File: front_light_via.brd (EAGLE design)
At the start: 60 x 73 mm, 9 parts

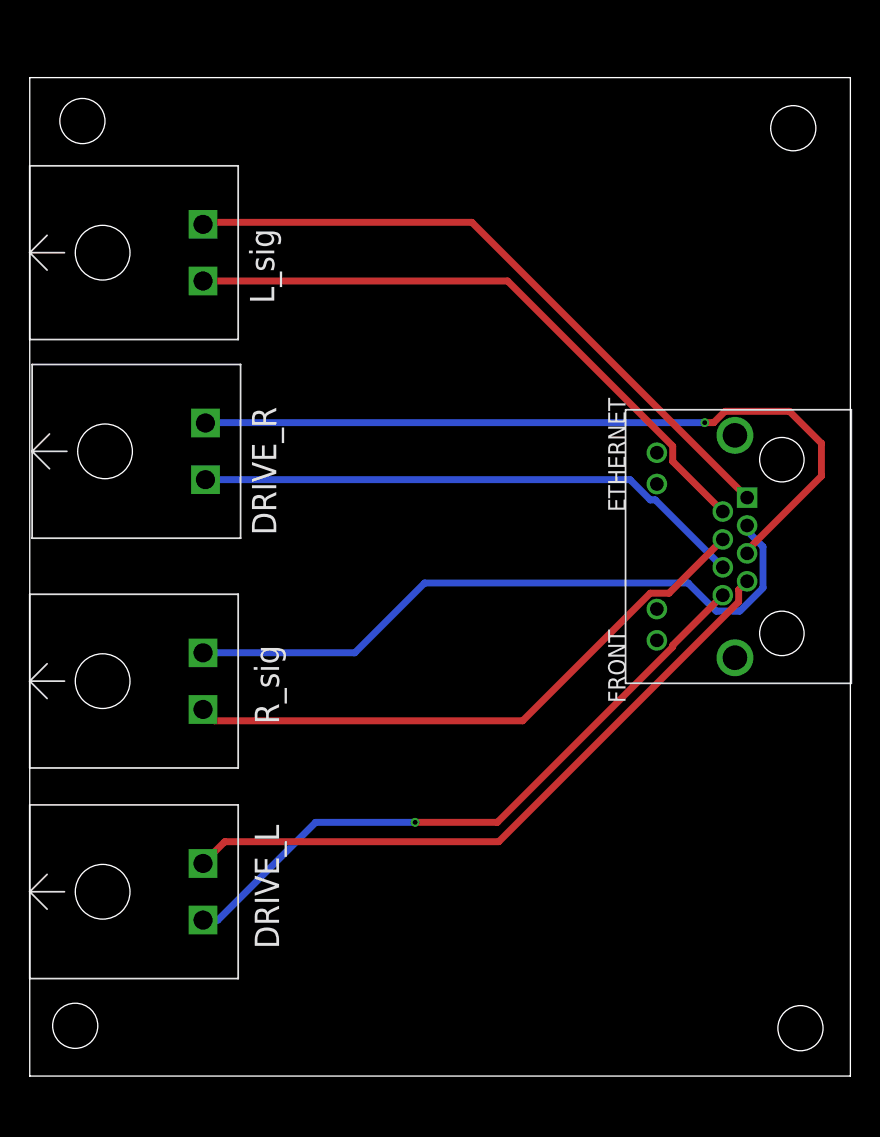
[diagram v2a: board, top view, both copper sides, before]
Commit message: correct all routing errors
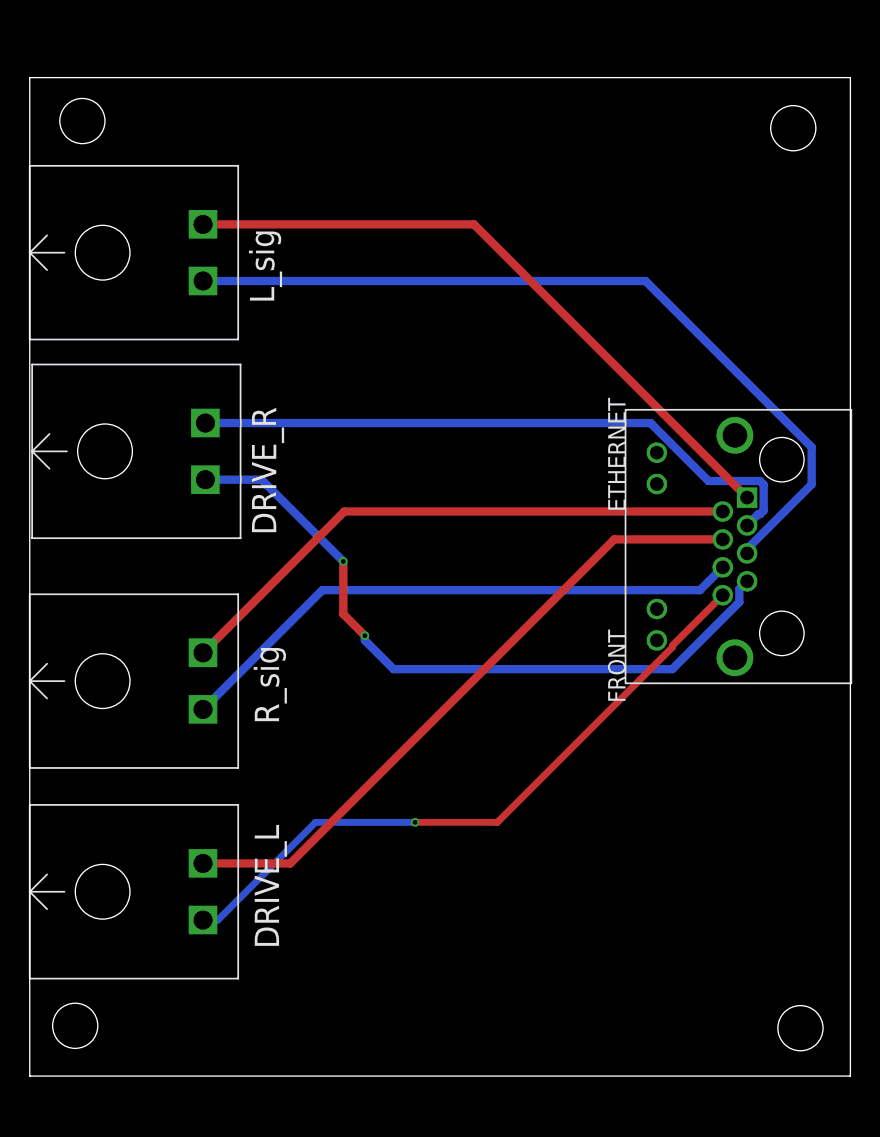
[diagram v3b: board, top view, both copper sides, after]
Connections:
- removed net BLIINK_R: FRONT.P$4, U$3.G/LOW
- removed net BLINK_L: FRONT.P$2, U$4.G/LOW
- removed net DRIVING_R: FRONT.P$6, U$2.G/LOW
- removed net N$3: FRONT.P$3, U$3.V/SIG
- removed net N$7 (its old number): FRONT.P$7, U$1.V/SIG
- new net DRIVING_RIGHT: FRONT.P$7, U$2.G/LOW
- new net L_SIG: FRONT.P$5, U$4.G/LOW
- new net N$4: FRONT.P$4, U$1.V/SIG
- new net N$6: FRONT.P$2, U$3.V/SIG
- new net R_SIG: FRONT.P$6, U$3.G/LOW
- net N$5: now also FRONT.P$3; no longer FRONT.P$5
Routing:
- net L_SIG: track 0.00 -> 59.3 mm
- net DRIVING_RIGHT: track 0.00 -> 51.0 mm, vias 0 -> 2
- net N$3: track 49.7 -> 0.00 mm
- net N$7 (its old number): track 48.8 -> 0.00 mm
- net N$4: track 0.00 -> 47.8 mm
- net BLINK_L: track 45.6 -> 0.00 mm
- net BLIINK_R: track 43.8 -> 0.00 mm
- net R_SIG: track 0.00 -> 42.3 mm
- net N$6: track 0.00 -> 42.3 mm
- net DRIVING_R: track 40.5 -> 0.00 mm
- net N$5: track 56.6 -> 46.2 mm, vias 1 -> 0
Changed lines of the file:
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@@
 <?xml version="1.0" encoding="utf-8"?>
 <!DOCTYPE eagle SYSTEM "eagle.dtd">
-<eagle version="8.6.1">
+<eagle version="9.0.0">
 <drawing>
 <settings>
@@
 </elements>
 <signals>
-<signal name="N$1">
-<contactref element="FRONT" pad="P$1"/>
-<wire x1="52.45" y1="42.295" x2="32.325" y2="62.42" width="0.508" layer="1"/>
-<contactref element="U$4" pad="V/SIG"/>
-<wire x1="32.325" y1="62.42" x2="12.82" y2="62.42" width="0.508" layer="1"/>
-<wire x1="12.82" y1="62.42" x2="12.67" y2="62.27" width="0.508" layer="1"/>
-</signal>
-<signal name="BLINK_L">
-<contactref element="FRONT" pad="P$2"/>
-<wire x1="50.67" y1="41.275" x2="47.0104" y2="44.9346" width="0.508" layer="1"/>
-<wire x1="47.0104" y1="44.9346" x2="47.0104" y2="46.05565625" width="0.508" layer="1"/>
-<contactref element="U$4" pad="G/LOW"/>
-<wire x1="34.93605625" y1="58.13" x2="12.67" y2="58.13" width="0.508" layer="1"/>
-<wire x1="47.0104" y1="46.05565625" x2="34.93605625" y2="58.13" width="0.508" layer="1"/>
-</signal>
-<signal name="N$3">
-<contactref element="FRONT" pad="P$3"/>
-<wire x1="53.6104" y1="38.69565625" x2="53.6104" y2="35.69434375" width="0.508" layer="16"/>
-<wire x1="52.45" y1="40.255" x2="52.45" y2="39.85605625" width="0.508" layer="16"/>
-<wire x1="48.13394375" y1="36.05" x2="28.875" y2="36.05" width="0.508" layer="16"/>
-<wire x1="52.45" y1="39.85605625" x2="53.6104" y2="38.69565625" width="0.508" layer="16"/>
-<wire x1="50.18934375" y1="33.9946" x2="48.13394375" y2="36.05" width="0.508" layer="16"/>
-<wire x1="53.6104" y1="35.69434375" x2="51.91065625" y2="33.9946" width="0.508" layer="16"/>
-<wire x1="51.91065625" y1="33.9946" x2="50.18934375" y2="33.9946" width="0.508" layer="16"/>
-<contactref element="U$3" pad="V/SIG"/>
-<wire x1="23.77" y1="30.945" x2="12.67" y2="30.945" width="0.508" layer="16"/>
-<wire x1="28.875" y1="36.05" x2="23.77" y2="30.945" width="0.508" layer="16"/>
-</signal>
-<signal name="BLIINK_R">
-<contactref element="FRONT" pad="P$4"/>
-<wire x1="50.67" y1="39.235" x2="46.7404" y2="35.3054" width="0.508" layer="1"/>
-<wire x1="46.7404" y1="35.3054" x2="45.36934375" y2="35.3054" width="0.508" layer="1"/>
-<wire x1="45.36934375" y1="35.3054" x2="36.03894375" y2="25.975" width="0.508" layer="1"/>
-<contactref element="U$3" pad="G/LOW"/>
-<wire x1="36.03894375" y1="25.975" x2="13.5" y2="25.975" width="0.508" layer="1"/>
-<wire x1="13.5" y1="25.975" x2="12.67" y2="26.805" width="0.508" layer="1"/>
-</signal>
-<signal name="N$5">
-<contactref element="FRONT" pad="P$5"/>
-<via x="49.35" y="47.775" extent="1-16" drill="0.35"/>
-<wire x1="57.885" y1="43.86585" x2="57.885" y2="46.26415" width="0.508" layer="1"/>
-<wire x1="52.45" y1="38.215" x2="52.45" y2="38.43085" width="0.508" layer="1"/>
-<wire x1="52.45" y1="38.43085" x2="57.885" y2="43.86585" width="0.508" layer="1"/>
-<wire x1="57.885" y1="46.26415" x2="55.54775" y2="48.6014" width="0.508" layer="1"/>
-<wire x1="55.54775" y1="48.6014" x2="50.832475" y2="48.6014" width="0.508" layer="1"/>
-<wire x1="50.832475" y1="48.6014" x2="50.006075" y2="47.775" width="0.508" layer="1"/>
-<wire x1="50.006075" y1="47.775" x2="49.35" y2="47.775" width="0.508" layer="1"/>
-<wire x1="49.35" y1="47.775" x2="12.85" y2="47.775" width="0.508" layer="16"/>
-<contactref element="U$2" pad="V/SIG"/>
-<wire x1="12.845" y1="47.745" x2="12.85" y2="47.775" width="0" layer="19" extent="16-16"/>
-</signal>
-<signal name="DRIVING_R">
-<contactref element="FRONT" pad="P$6"/>
-<contactref element="U$2" pad="G/LOW"/>
-<wire x1="45.7404" y1="42.1246" x2="45.36934375" y2="42.1246" width="0.508" layer="16"/>
-<wire x1="43.88894375" y1="43.605" x2="12.845" y2="43.605" width="0.508" layer="16"/>
-<wire x1="45.36934375" y1="42.1246" x2="43.88894375" y2="43.605" width="0.508" layer="16"/>
-<wire x1="50.67" y1="37.195" x2="45.7404" y2="42.1246" width="0.508" layer="16"/>
-</signal>
-<signal name="N$7">
-<contactref element="FRONT" pad="P$7"/>
-<wire x1="52.45" y1="36.175" x2="51.8304" y2="35.5554" width="0.508" layer="1"/>
-<wire x1="51.8304" y1="35.5554" x2="51.8304" y2="34.67434375" width="0.508" layer="1"/>
-<wire x1="51.8304" y1="34.67434375" x2="34.29105625" y2="17.135" width="0.508" layer="1"/>
-<contactref element="U$1" pad="V/SIG"/>
-<wire x1="34.29105625" y1="17.135" x2="14.26" y2="17.135" width="0.508" layer="1"/>
-<wire x1="14.26" y1="17.135" x2="12.67" y2="15.545" width="0.508" layer="1"/>
-</signal>
 <signal name="DRIVING_L">
 <contactref element="FRONT" pad="P$8"/>
@@
 <wire x1="13.755" y1="11.405" x2="12.67" y2="11.405" width="0.508" layer="16"/>
 </signal>
+<signal name="DRIVING_RIGHT">
+<contactref element="FRONT" pad="P$7"/>
+<contactref element="U$2" pad="G/LOW"/>
+<wire x1="52.45" y1="36.175" x2="51.8812" y2="35.6062" width="0.6096" layer="16"/>
+<wire x1="51.8812" y1="35.6062" x2="51.8812" y2="34.6533" width="0.6096" layer="16"/>
+<wire x1="51.8812" y1="34.6533" x2="46.9779" y2="29.75" width="0.6096" layer="16"/>
+<wire x1="46.9779" y1="29.75" x2="26.6" y2="29.75" width="0.6096" layer="16"/>
+<wire x1="26.6" y1="29.75" x2="24.5" y2="31.85" width="0.6096" layer="16"/>
+<wire x1="24.5" y1="31.85" x2="24.5" y2="32.2" width="0.6096" layer="16"/>
+<via x="24.5" y="32.2" extent="1-16" drill="0.35"/>
+<wire x1="24.5" y1="32.2" x2="22.925" y2="33.775" width="0.6096" layer="1"/>
+<wire x1="22.925" y1="33.775" x2="22.925" y2="37.625" width="0.6096" layer="1"/>
+<via x="22.925" y="37.625" extent="1-16" drill="0.35"/>
+<wire x1="22.925" y1="37.625" x2="16.945" y2="43.605" width="0.6096" layer="16"/>
+<wire x1="16.945" y1="43.605" x2="12.845" y2="43.605" width="0.6096" layer="16"/>
+</signal>
+<signal name="R_SIG">
+<contactref element="U$3" pad="G/LOW"/>
+<contactref element="FRONT" pad="P$6"/>
+<wire x1="50.67" y1="37.195" x2="49" y2="35.525" width="0.6096" layer="16"/>
+<wire x1="21.39" y1="35.525" x2="12.67" y2="26.805" width="0.6096" layer="16"/>
+<wire x1="49" y1="35.525" x2="21.39" y2="35.525" width="0.6096" layer="16"/>
+</signal>
+<signal name="L_SIG">
+<contactref element="U$4" pad="G/LOW"/>
+<contactref element="FRONT" pad="P$5"/>
+<wire x1="52.45" y1="38.5421" x2="52.45" y2="38.215" width="0.6096" layer="16"/>
+<wire x1="57.1738" y1="45.9695625" x2="57.1738" y2="43.2659" width="0.6096" layer="16"/>
+<wire x1="57.1738" y1="43.2659" x2="52.45" y2="38.5421" width="0.6096" layer="16"/>
+<wire x1="45.0133625" y1="58.13" x2="57.1738" y2="45.9695625" width="0.6096" layer="16"/>
+<wire x1="12.67" y1="58.13" x2="45.0133625" y2="58.13" width="0.6096" layer="16"/>
+</signal>
+<signal name="N$4">
+<contactref element="FRONT" pad="P$4"/>
+<contactref element="U$1" pad="V/SIG"/>
+<wire x1="12.67" y1="15.545" x2="19.045" y2="15.545" width="0.6096" layer="1"/>
+<wire x1="42.735" y1="39.235" x2="50.67" y2="39.235" width="0.6096" layer="1"/>
+<wire x1="19.045" y1="15.545" x2="42.735" y2="39.235" width="0.6096" layer="1"/>
+</signal>
+<signal name="N$5">
+<contactref element="FRONT" pad="P$3"/>
+<contactref element="U$2" pad="V/SIG"/>
+<wire x1="53.39338125" y1="41.0838" x2="53.6612" y2="41.35161875" width="0.6096" layer="16"/>
+<wire x1="53.6612" y1="41.35161875" x2="53.6612" y2="43.23838125" width="0.6096" layer="16"/>
+<wire x1="53.6612" y1="43.23838125" x2="53.39338125" y2="43.5062" width="0.6096" layer="16"/>
+<wire x1="52.45" y1="40.255" x2="53.2788" y2="41.0838" width="0.6096" layer="16"/>
+<wire x1="53.2788" y1="41.0838" x2="53.39338125" y2="41.0838" width="0.6096" layer="16"/>
+<wire x1="53.39338125" y1="43.5062" x2="49.6317" y2="43.5062" width="0.6096" layer="16"/>
+<wire x1="49.6317" y1="43.5062" x2="45.3929" y2="47.745" width="0.6096" layer="16"/>
+<wire x1="45.3929" y1="47.745" x2="12.845" y2="47.745" width="0.6096" layer="16"/>
+</signal>
+<signal name="N$6">
+<contactref element="FRONT" pad="P$2"/>
+<contactref element="U$3" pad="V/SIG"/>
+<wire x1="50.67" y1="41.275" x2="23" y2="41.275" width="0.6096" layer="1"/>
+<wire x1="23" y1="41.275" x2="12.67" y2="30.945" width="0.6096" layer="1"/>
+</signal>
+<signal name="N$7">
+<contactref element="FRONT" pad="P$1"/>
+<contactref element="U$4" pad="V/SIG"/>
+<wire x1="12.67" y1="62.27" x2="32.475" y2="62.27" width="0.6096" layer="1"/>
+<wire x1="32.475" y1="62.27" x2="52.45" y2="42.295" width="0.6096" layer="1"/>
+</signal>
 </signals>
